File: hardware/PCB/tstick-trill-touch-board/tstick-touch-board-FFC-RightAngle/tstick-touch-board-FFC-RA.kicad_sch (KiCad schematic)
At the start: 12 parts, among them J1 Conn_01x32

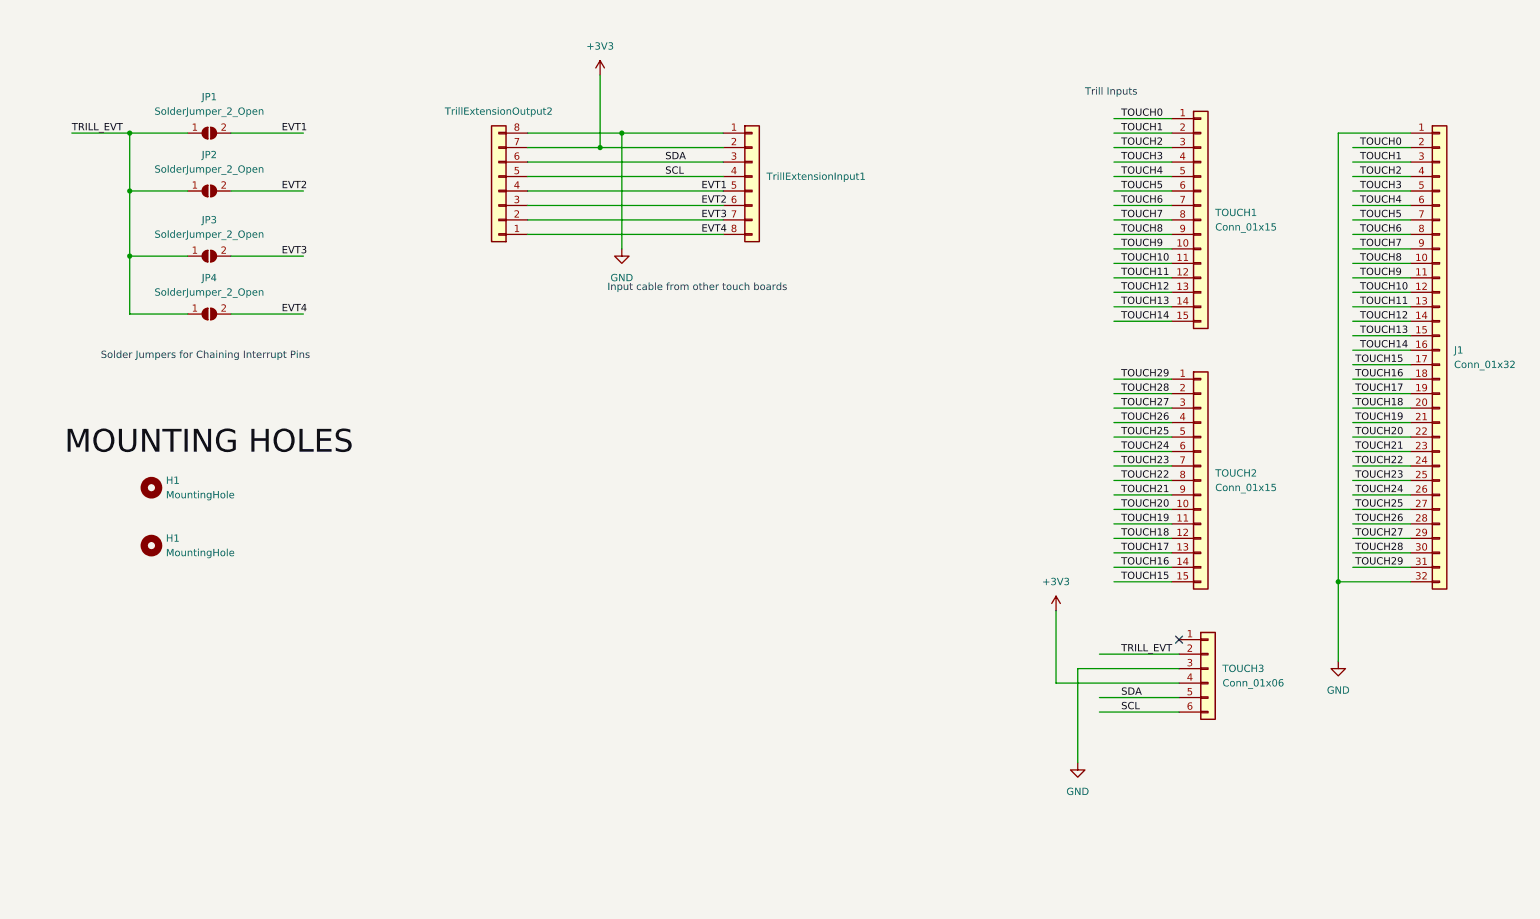
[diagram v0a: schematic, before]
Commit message: cleaned up the pcb designs for the touch extension boards, created BOM and gerber files for fabrication and assembly
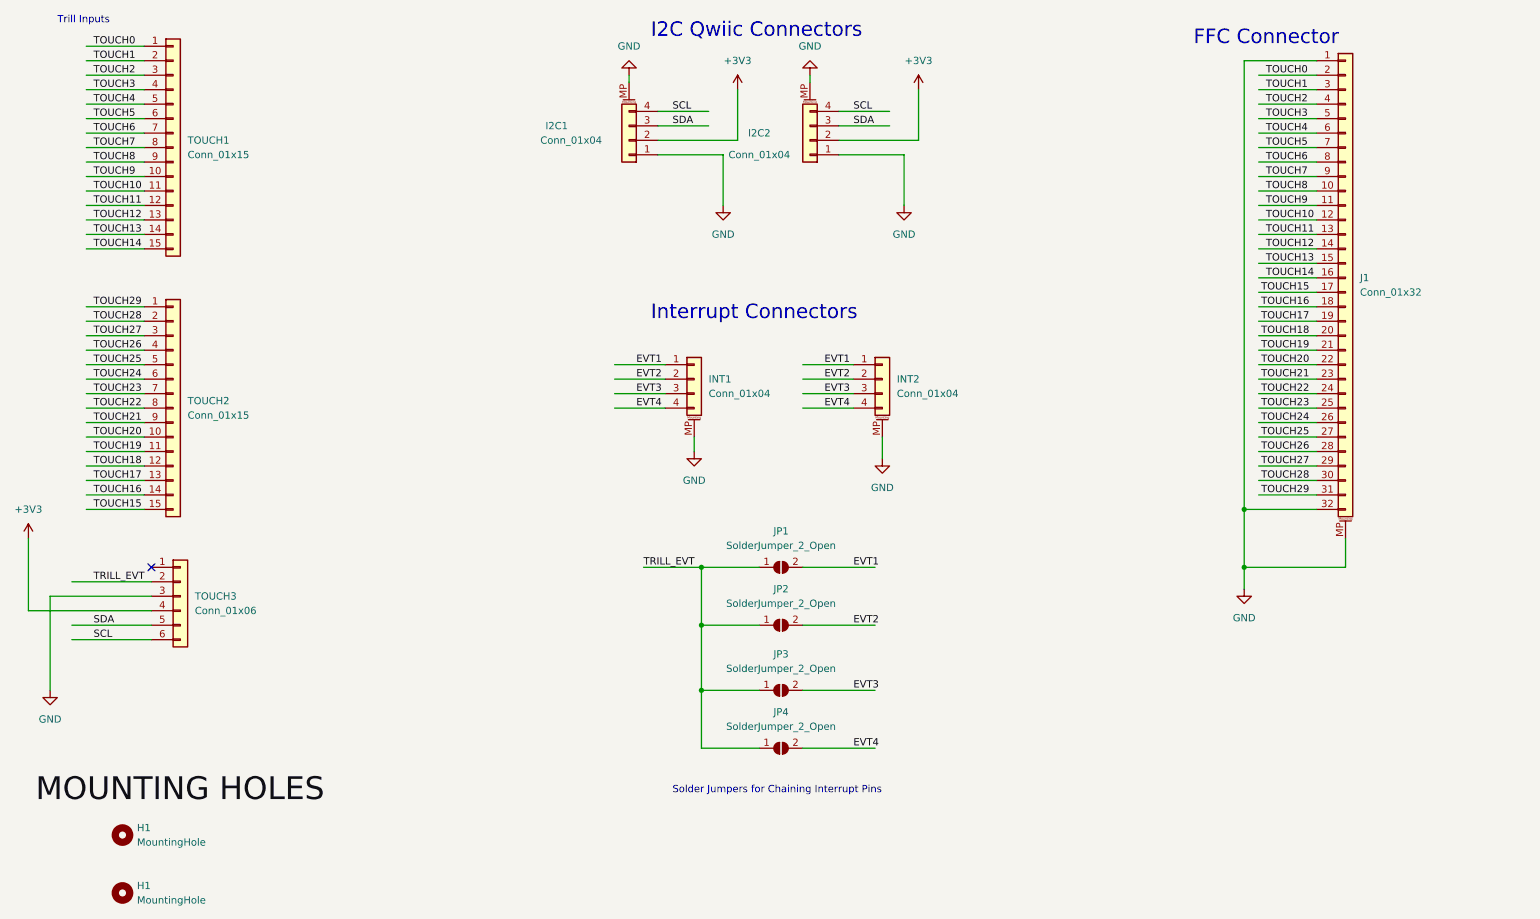
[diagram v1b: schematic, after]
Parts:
- removed TrillExtensionInput1, TrillExtensionOutput2: Conn_01x08, Connector_JST:JST_SHL_SM08B-SHLS-TF_1x08-1MP_P1.00mm_Horizontal, symbol Connector_Generic:Conn_01x08
- added I2C1, I2C2, INT1, INT2: Conn_01x04, Connector_JST:JST_SH_SM04B-SRSS-TB_1x04-1MP_P1.00mm_Horizontal, symbol Connector_Generic_MountingPin:Conn_01x04_MountingPin
- J1: footprint molex_ffc_footprints:CON_541323262_MOL -> molex-ffc-connectors:CON_541323262_MOL; symbol Connector_Generic:Conn_01x32 -> Connector_Generic_MountingPin:Conn_01x32_MountingPin
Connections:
- net +3V3: now also I2C1.2 (Pin_2), I2C2.2 (Pin_2)
- net EVT1: now also INT1.1 (Pin_1), INT2.1 (Pin_1)
- net EVT2: now also INT1.2 (Pin_2), INT2.2 (Pin_2)
- net EVT3: now also INT1.3 (Pin_3), INT2.3 (Pin_3)
- net EVT4: now also INT1.4 (Pin_4), INT2.4 (Pin_4)
- net GND: now also J1.MP (MountPin), I2C1.1 (Pin_1), I2C1.MP (MountPin), I2C2.1 (Pin_1), I2C2.MP (MountPin), INT1.MP (MountPin), INT2.MP (MountPin)
- net SCL: now also I2C1.4 (Pin_4), I2C2.4 (Pin_4)
- net SDA: now also I2C1.3 (Pin_3), I2C2.3 (Pin_3)
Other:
- note added: "FFC Connector"
- note added: "I2C Qwiic Connectors"
- note added: "Interrupt Connectors"
- note removed: "Input cable from other touch boards"
- company: (none) -> Input Devices and Musical Interaction Lab, McGill University
- title: (none) -> T-stick Trill Touch Extension Board vFFC
- moved on the sheet: H1, JP1, JP2, JP3, JP4, TOUCH1, TOUCH2, TOUCH3
